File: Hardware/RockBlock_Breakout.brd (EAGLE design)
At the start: 25.4 x 53 mm, 24 parts, among them J1 CONN_62.54, J2 CONN_82.54, U1 ATMEGA328P_TQFP, U4 TPS61027DRC, Y1 16MHz

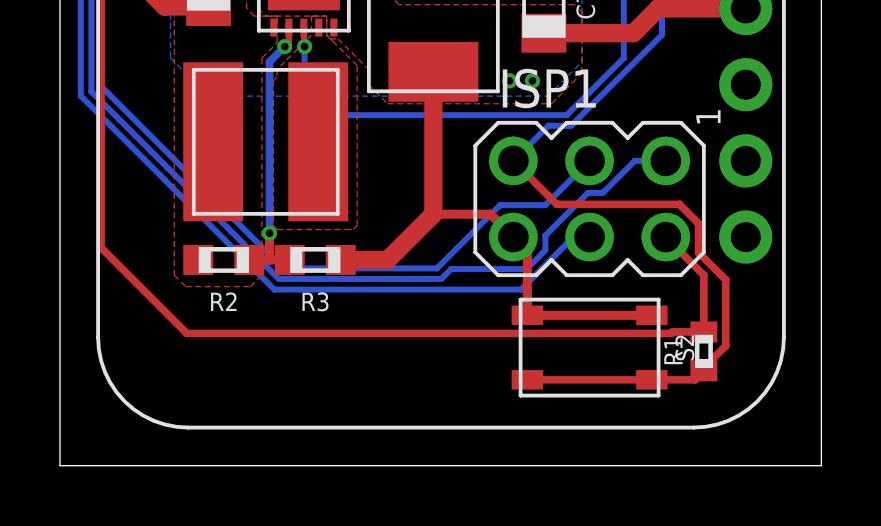
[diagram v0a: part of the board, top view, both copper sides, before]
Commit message: Aligned buttons on RockBlock breakout
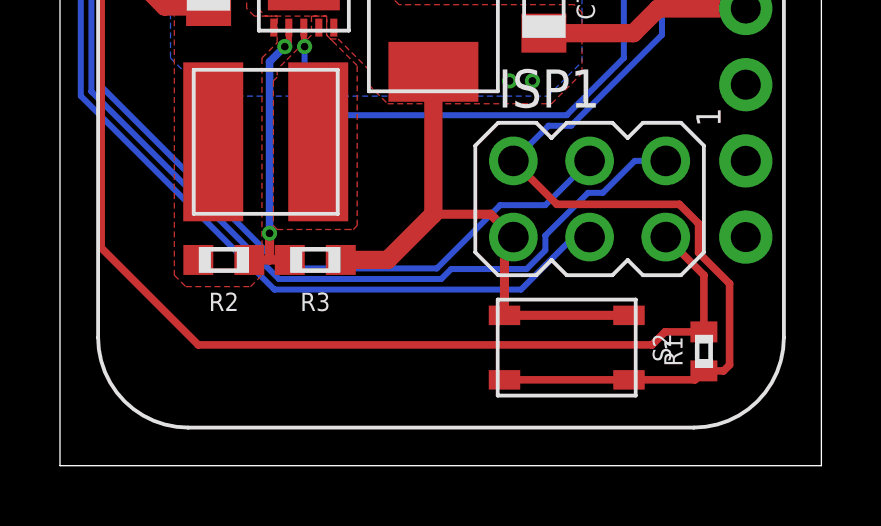
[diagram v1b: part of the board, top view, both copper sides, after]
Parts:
- moved S2 0.76 mm to (16.9, 3.94)
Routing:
- net RST: track 40.2 -> 41.4 mm
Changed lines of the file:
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@@
 <attribute name="NAME" x="20.066" y="48.387" size="0.6096" layer="25" font="vector" ratio="15" rot="R270" align="center"/>
 </element>
-<element name="S2" library="bschulz" package="SWITCH_4.2X3.2" value="BUTTON4.2X3.2" x="17.653" y="3.937" smashed="yes" rot="R180">
-<attribute name="DIGIKEY" value="CKN10504CT-ND" x="-29.337" y="53.467" size="1.778" layer="27" rot="R180" display="off"/>
-<attribute name="MF" value="C&amp;K" x="-29.337" y="53.467" size="1.778" layer="27" rot="R180" display="off"/>
-<attribute name="MPN" value="PTS810 SJG 250 SMTR LFS" x="-29.337" y="53.467" size="1.778" layer="27" rot="R180" display="off"/>
-<attribute name="NAME" x="20.828" y="3.937" size="0.6096" layer="25" font="vector" ratio="15" rot="R270" align="center"/>
+<element name="S2" library="bschulz" package="SWITCH_4.2X3.2" value="BUTTON4.2X3.2" x="16.891" y="3.937" smashed="yes" rot="R180">
+<attribute name="DIGIKEY" value="CKN10504CT-ND" x="-30.099" y="53.467" size="1.778" layer="27" rot="R180" display="off"/>
+<attribute name="MF" value="C&amp;K" x="-30.099" y="53.467" size="1.778" layer="27" rot="R180" display="off"/>
+<attribute name="MPN" value="PTS810 SJG 250 SMTR LFS" x="-30.099" y="53.467" size="1.778" layer="27" rot="R180" display="off"/>
+<attribute name="NAME" x="20.066" y="3.937" size="0.6096" layer="25" font="vector" ratio="15" rot="R270" align="center"/>
 </element>
 <element name="U1" library="bschulz" package="TQFP32-08" package3d_urn="urn:adsk.eagle:package:38945/1" value="ATMEGA328P_TQFP" x="14.478" y="27.686" smashed="yes" rot="R270">
@@
 <wire x1="3.175" y1="49.784" x2="5.969" y2="49.784" width="0.4064" layer="16"/>
 <wire x1="1.2954" y1="47.9044" x2="3.175" y2="49.784" width="0.4064" layer="16"/>
-<wire x1="15.113" y1="7.62" x2="15.578" y2="7.155" width="0.3048" layer="1"/>
-<wire x1="15.578" y1="7.155" x2="15.578" y2="5.012" width="0.3048" layer="1"/>
+<wire x1="15.113" y1="7.62" x2="14.816" y2="7.323" width="0.3048" layer="1"/>
+<wire x1="14.816" y1="7.323" x2="14.816" y2="5.012" width="0.3048" layer="1"/>
 <wire x1="15.113" y1="7.62" x2="14.351" y2="8.382" width="0.3048" layer="1"/>
 <wire x1="14.351" y1="8.382" x2="12.446" y2="8.382" width="0.3048" layer="1"/>
-<wire x1="15.578" y1="5.012" x2="19.728" y2="5.012" width="0.3048" layer="1"/>
+<wire x1="14.816" y1="5.012" x2="18.966" y2="5.012" width="0.3048" layer="1"/>
 <wire x1="24.2062" y1="31.75" x2="18.669" y2="31.75" width="0.3048" layer="1"/>
 <wire x1="17.202" y1="30.283" x2="15.678" y2="30.283" width="0.3048" layer="1"/>
@@
 <wire x1="21.463" y1="6.35" x2="20.193" y2="7.62" width="0.254" layer="1"/>
 <wire x1="2.54" y1="22.86" x2="1.3716" y2="21.6916" width="0.254" layer="1"/>
-<wire x1="20.36873125" y1="4.4076" x2="20.42113125" y2="4.46" width="0.254" layer="1"/>
-<wire x1="20.42113125" y1="4.46" x2="21.463" y2="4.46" width="0.254" layer="1"/>
-<wire x1="4.2284" y1="4.4076" x2="20.36873125" y2="4.4076" width="0.254" layer="1"/>
-<wire x1="1.3716" y1="7.2644" x2="4.2284" y2="4.4076" width="0.254" layer="1"/>
+<wire x1="19.73373125" y1="4.0266" x2="20.16713125" y2="4.46" width="0.254" layer="1"/>
+<wire x1="20.16713125" y1="4.46" x2="21.463" y2="4.46" width="0.254" layer="1"/>
+<wire x1="4.6094" y1="4.0266" x2="19.73373125" y2="4.0266" width="0.254" layer="1"/>
+<wire x1="1.3716" y1="7.2644" x2="4.6094" y2="4.0266" width="0.254" layer="1"/>
 <wire x1="1.3716" y1="21.6916" x2="1.3716" y2="7.2644" width="0.254" layer="1"/>
 <wire x1="13.12" y1="21.59" x2="12.446" y2="20.916" width="0.254" layer="1"/>
@@
 <wire x1="19.793" y1="28.086" x2="18.7706" y2="28.086" width="0.2" layer="1"/>
 <wire x1="20.066" y1="27.813" x2="19.793" y2="28.086" width="0.2" layer="1"/>
-<wire x1="15.578" y1="2.862" x2="19.728" y2="2.862" width="0.254" layer="1"/>
-<wire x1="19.728" y1="2.862" x2="21.165" y2="2.862" width="0.254" layer="1"/>
+<wire x1="14.816" y1="2.862" x2="18.966" y2="2.862" width="0.254" layer="1"/>
+<wire x1="18.966" y1="2.862" x2="21.165" y2="2.862" width="0.254" layer="1"/>
 <wire x1="21.165" y1="2.862" x2="21.463" y2="3.16" width="0.254" layer="1"/>
 <wire x1="21.2852" y1="8.07240625" x2="20.64540625" y2="8.7122" width="0.254" layer="1"/>
-<wire x1="21.463" y1="3.16" x2="21.463" y2="3.26486875" width="0.254" layer="1"/>
-<wire x1="21.463" y1="3.26486875" x2="22.1924" y2="3.99426875" width="0.254" layer="1"/>
+<wire x1="22.3194" y1="3.35926875" x2="22.12013125" y2="3.16" width="0.254" layer="1"/>
+<wire x1="21.463" y1="3.16" x2="22.12013125" y2="3.16" width="0.254" layer="1"/>
 <wire x1="21.2852" y1="7.1025375" x2="21.2852" y2="8.07240625" width="0.254" layer="1"/>
 <wire x1="20.64540625" y1="8.7122" x2="16.5608" y2="8.7122" width="0.254" layer="1"/>
-<wire x1="22.1924" y1="3.99426875" x2="22.1924" y2="6.1953375" width="0.254" layer="1"/>
-<wire x1="22.1924" y1="6.1953375" x2="21.2852" y2="7.1025375" width="0.254" layer="1"/>
+<wire x1="22.3194" y1="3.35926875" x2="22.3194" y2="6.0683375" width="0.254" layer="1"/>
+<wire x1="22.3194" y1="6.0683375" x2="21.2852" y2="7.1025375" width="0.254" layer="1"/>
 <wire x1="16.5608" y1="8.7122" x2="15.113" y2="10.16" width="0.254" layer="1"/>
 </signal>

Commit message: Routing cleanup
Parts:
- moved L2 1.27 mm to (6.86, 9.53)
- moved J1 1.17 mm to (8.51, 42.3)
- moved C1 1.14 mm to (14.0, 20.4)
- moved C2 1.14 mm to (4.95, 15.1)
- moved C3 1.14 mm to (14.9, 33.3)
- moved C5 1.14 mm to (12.4, 15.0)
- moved C7 1.14 mm to (16.1, 14.2)
- moved D5 1.14 mm to (17.0, 41.0)
- moved ISP1 1.14 mm to (17.7, 7.75)
- moved J2 1.14 mm to (5.97, 39.8)
- moved R4 1.14 mm to (16.9, 44.7)
- moved R42 1.14 mm to (18.5, 37.8)
- moved R43 1.14 mm to (17.4, 37.8)
- moved R44 1.14 mm to (16.3, 37.8)
- moved S1 1.14 mm to (16.9, 47.2)
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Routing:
- net 5V: track 119.9 -> 119.4 mm
- net GND: track 140.8 -> 141.3 mm
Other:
- board size 25.4 x 53 mm -> 24.9 x 51.1 mm
